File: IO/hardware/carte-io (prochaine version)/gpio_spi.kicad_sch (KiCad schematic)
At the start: 19 parts, among them J20 114020164, J21 114020164, J22 114020164, J28 114020164, J29 114020164, J30 114020164, U24 CM1293A-04SO

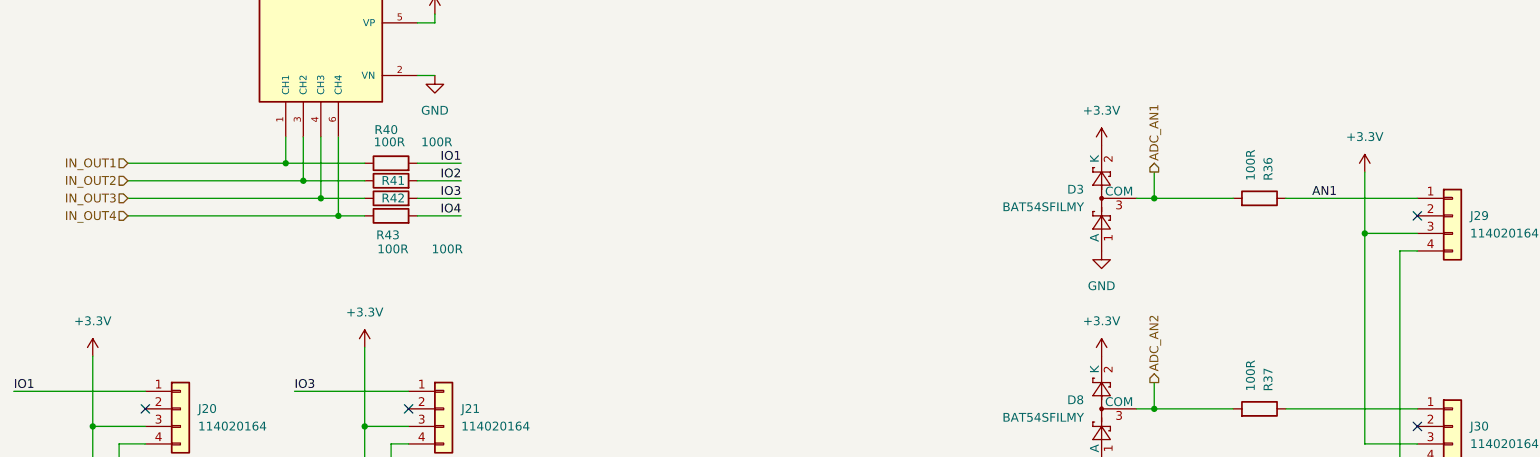
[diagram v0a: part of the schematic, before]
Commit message: Recuperation de la carte IO perdue lors de la suppression des 3 derniers commit
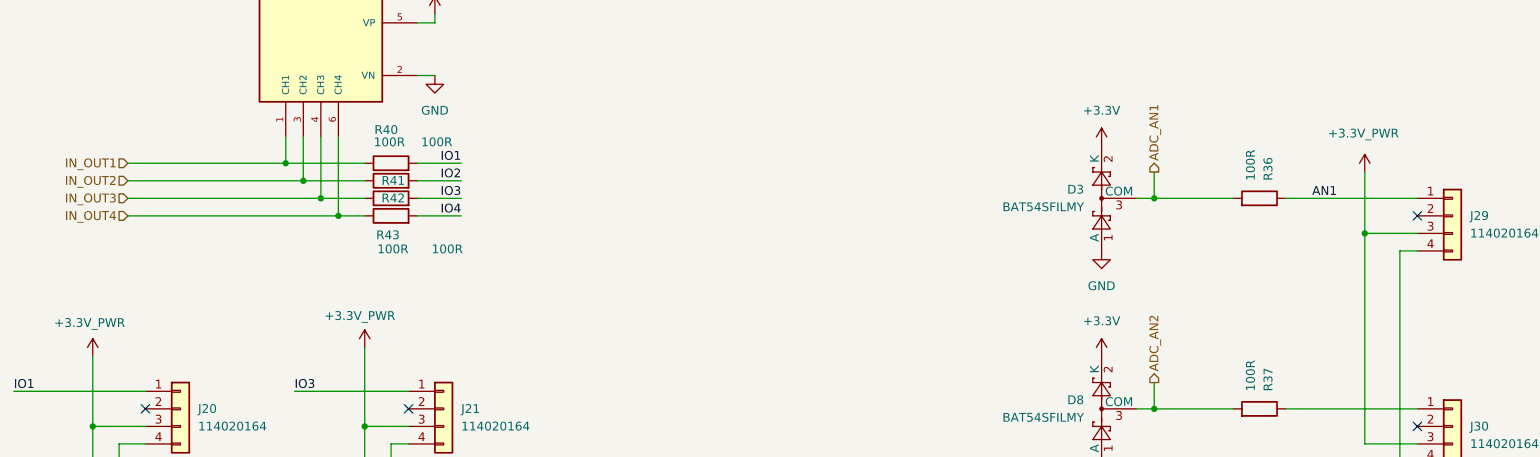
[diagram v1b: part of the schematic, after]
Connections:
- net +3.3V: no longer J20.3 (Pin_3), J21.3 (Pin_3), J22.3 (Pin_3), J28.3 (Pin_3), J29.3 (Pin_3), J30.3 (Pin_3)
- new net +3.3V_PWR: J20.3 (Pin_3), J21.3 (Pin_3), J22.3 (Pin_3), J28.3 (Pin_3), J29.3 (Pin_3), J30.3 (Pin_3)
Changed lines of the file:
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@@
 		(on_board yes)
 		(dnp no)
-		(fields_autoplaced yes)
 		(property "Reference" "#PWR106"
 			(at 215.9 57.15 0)
@@
 			)
 		)
-		(property "Value" "+3.3V"
-			(at 215.9 48.26 0)
-			(effects
-				(font
-					(size 1.27 1.27)
-				)
+		(property "Value" "+3.3V_PWR"
+			(at 210.566 47.752 0)
+			(effects
+				(font
+					(size 1.27 1.27)
+				)
+				(justify left)
 			)
 		)
@@
 		(on_board yes)
 		(dnp no)
-		(fields_autoplaced yes)
 		(property "Reference" "#PWR0104"
 			(at 71.12 82.55 0)
@@
 			)
 		)
-		(property "Value" "+3.3V"
-			(at 71.12 73.66 0)
-			(effects
-				(font
-					(size 1.27 1.27)
-				)
+		(property "Value" "+3.3V_PWR"
+			(at 65.278 74.168 0)
+			(effects
+				(font
+					(size 1.27 1.27)
+				)
+				(justify left)
 			)
 		)
@@
 		(on_board yes)
 		(dnp no)
-		(fields_autoplaced yes)
 		(property "Reference" "#PWR0103"
 			(at 31.75 83.82 0)
@@
 			)
 		)
-		(property "Value" "+3.3V"
-			(at 31.75 74.93 0)
-			(effects
-				(font
-					(size 1.27 1.27)
-				)
-			)
-		)
+		(property "Value" "+3.3V_PWR"
+			(at 26.162 75.184 0)
+			(effects
+				(font
+					(size 1.27 1.27)
+				)
+				(justify left)
+			)
+		)
